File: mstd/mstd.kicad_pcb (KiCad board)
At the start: 4 copper layers, 96 x 96.3 mm, 92 parts, among them J1 PROG, Q2 2N7002, SW1 TSX101G100-250, U1 ICE40UP5K-SG48ITR, U10 74HCT05, U12 74HCT4066, U2 TLV70212DBVR, U3 TMI6050-33, U4 ESP32-WROOM-32E-N16, U5 74LVX3245MTCX, U6 74LVX3245MTCX, U7 SSD1306 OLED, U8 74HCT05, U9 APX803S-31SA

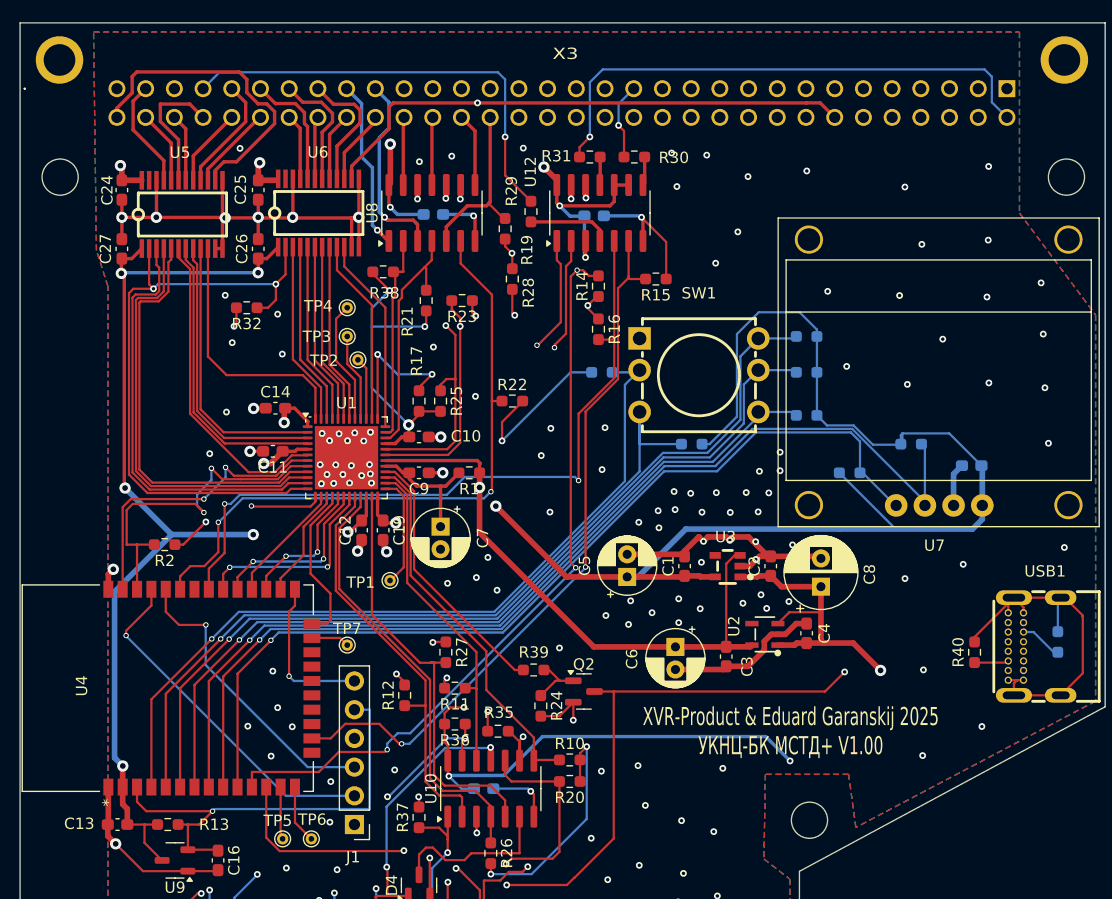
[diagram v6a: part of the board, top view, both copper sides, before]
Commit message: Fixes 74LVCX3245 package
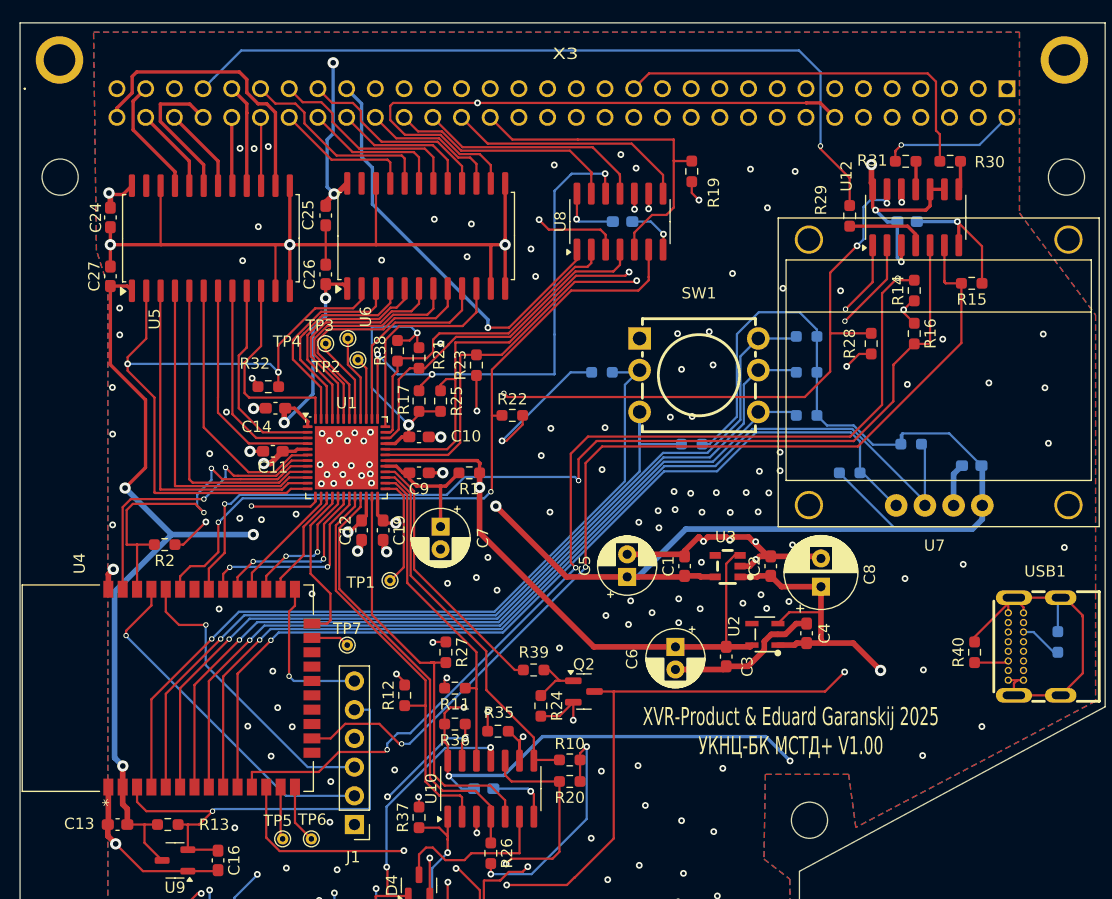
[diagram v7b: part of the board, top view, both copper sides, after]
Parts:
- U5, U6: footprint easyeda2kicad:TSSOP-24_L7.8-W4.4-P0.65-LS6.4-BL -> Package_SO:SOP-24_7.5x15.4mm_P1.27mm
- moved R28 32.3 mm to (122.3, 115.9), turned to 90 degrees
- moved R29 28.2 mm to (120.4, 104.6)
- moved R14 27.9 mm to (126.1, 111.2)
- moved R15 27.9 mm to (131.2, 110.5)
- moved R16 27.9 mm to (126.1, 115.0)
- moved R30 27.9 mm to (129.3, 99.7)
- moved R31 27.9 mm to (125.3, 99.7)
- moved U12 27.9 mm to (126.2, 104.7)
- moved C17 27.7 mm to (125.5, 105.1)
- moved R19 17.3 mm to (106.4, 100.6)
- moved C22 16.7 mm to (100.3, 105.1)
- moved U8 16.7 mm to (100.1, 105.1)
- moved U6 9.74 mm to (82.9, 106.3), turned to 90 degrees
- moved R32 7.24 mm to (69.0, 119.7)
- moved R38 7.10 mm to (80.4, 116.5), turned to -90 degrees
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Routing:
- net Net-(X3D-MON-DIS): track 47.4 -> 12.0 mm
- net /RUN: track 63.3 -> 96.5 mm, vias 3 -> 4
- net GND: track 217.9 -> 249.6 mm, vias 152 -> 162
- net Net-(X3D-BAS3-DIS): track 39.3 -> 69.7 mm
- net Net-(X3B-IAKN2): track 99.9 -> 129.1 mm
- net Net-(X3D-BAS-DIS): track 6.80 -> 34.8 mm, vias 1 -> 0
- net Net-(X4C-RUN1): track 90.5 -> 117.3 mm
- net Net-(X4C-RUN2): track 106.2 -> 132.2 mm
- net /ROM-DIS1: track 64.0 -> 88.9 mm
- net /ROM-DIS3: track 74.5 -> 98.9 mm
- net /ROM-DIS2: track 64.5 -> 88.5 mm
- net Net-(X3A-DIN): track 142.5 -> 160.2 mm
- net /IO/SYNC: track 29.6 -> 47.0 mm
- net Net-(X3A-RPLY): track 136.7 -> 151.8 mm
- net Net-(X3A-DOUT): track 117.3 -> 131.7 mm
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
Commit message: Finalized PCB
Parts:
- added JP1: SolderJumper_3_Bridged12, Jumper:SolderJumper-3_P1.3mm_Bridged12_RoundedPad1.0x1.5mm, B.Cu at (130.6, 122.2)
- added JP2: SolderJumper_3_Bridged12, Jumper:SolderJumper-3_P1.3mm_Bridged12_RoundedPad1.0x1.5mm, B.Cu at (130.6, 134.9)
- U7: footprint local:SDD1306 -> local:SDD1306-1
- moved R3 12.8 mm to (107.7, 128.6)
- moved R29 4.17 mm to (122.9, 101.3)
- moved C17 2.41 mm to (127.9, 105.1)
- moved R30 2.41 mm to (131.7, 99.7)
- moved U12 2.41 mm to (128.7, 104.7)
- moved R31 2.41 mm to (127.8, 99.7)
- moved C8 1.36 mm to (117.9, 138.7)
- moved C4 1.35 mm to (117.0, 142.8)
- moved U2 1.35 mm to (113.4, 142.9)
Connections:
- C15 pad 1: +3V3 -> Net-(JP2-C)
- C15 pad 2: GND -> Net-(JP1-C)
- U7 pad 1: +3V3 -> Net-(JP2-C)
- U7 pad 2: GND -> Net-(JP1-C)
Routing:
- net Net-(JP2-C): track 0.00 -> 8.94 mm
- net Net-(JP1-C): track 0.00 -> 8.37 mm
- net +5V: track 421.7 -> 428.1 mm
- net +3V3: track 390.5 -> 394.4 mm, vias 15 -> 17
- net /CPU/CIO1: track 89.5 -> 86.4 mm
- net /ROM-DIS3: track 98.9 -> 102.0 mm
- net GND: track 249.6 -> 246.8 mm, vias 162 -> 163
- net Net-(X3D-MON-DIS): track 12.0 -> 9.97 mm
- net /CPU/CIO2: track 81.4 -> 79.5 mm
- net Net-(R29-Pad1): track 7.11 -> 9.02 mm
- net Net-(Q2-D): track 126.8 -> 128.3 mm
- net Net-(X4C-RUN2): track 132.2 -> 133.7 mm
- net Net-(X4C-RUN1): track 117.3 -> 118.7 mm
- net /ROM-DIS1: track 88.9 -> 87.9 mm
- net Net-(X3D-BAS-DIS): track 34.8 -> 35.8 mm
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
